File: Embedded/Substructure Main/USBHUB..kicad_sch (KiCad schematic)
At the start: 19 parts, among them U4 USB2513B_Bi, Y1 24MHz 18pF

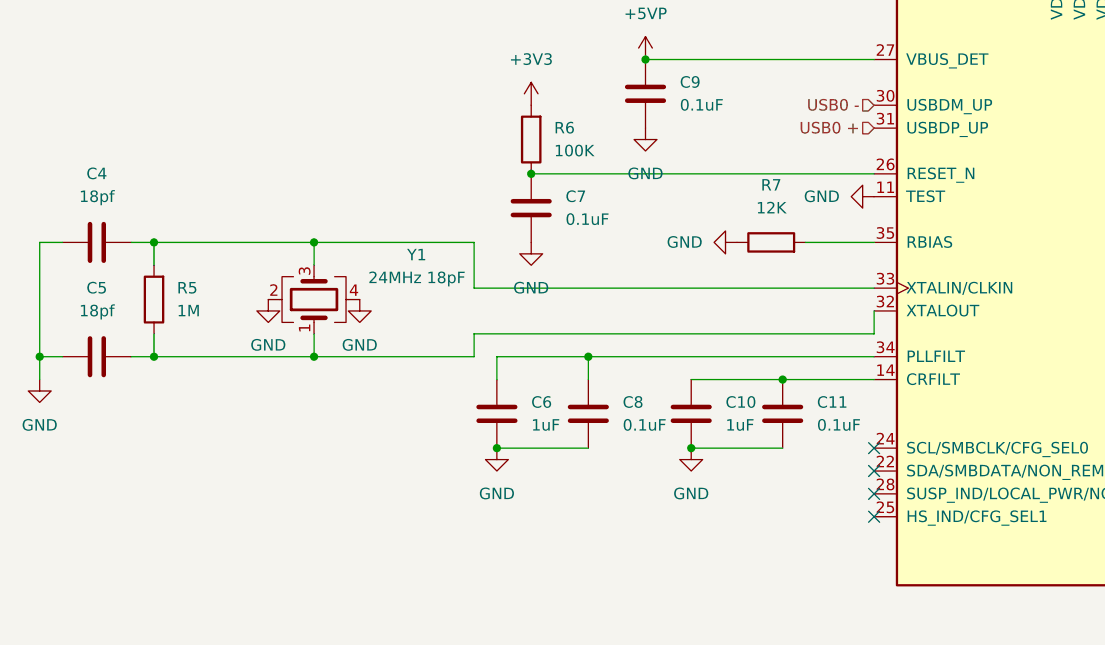
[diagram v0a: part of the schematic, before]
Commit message: Added LDOs and Modified Component Names
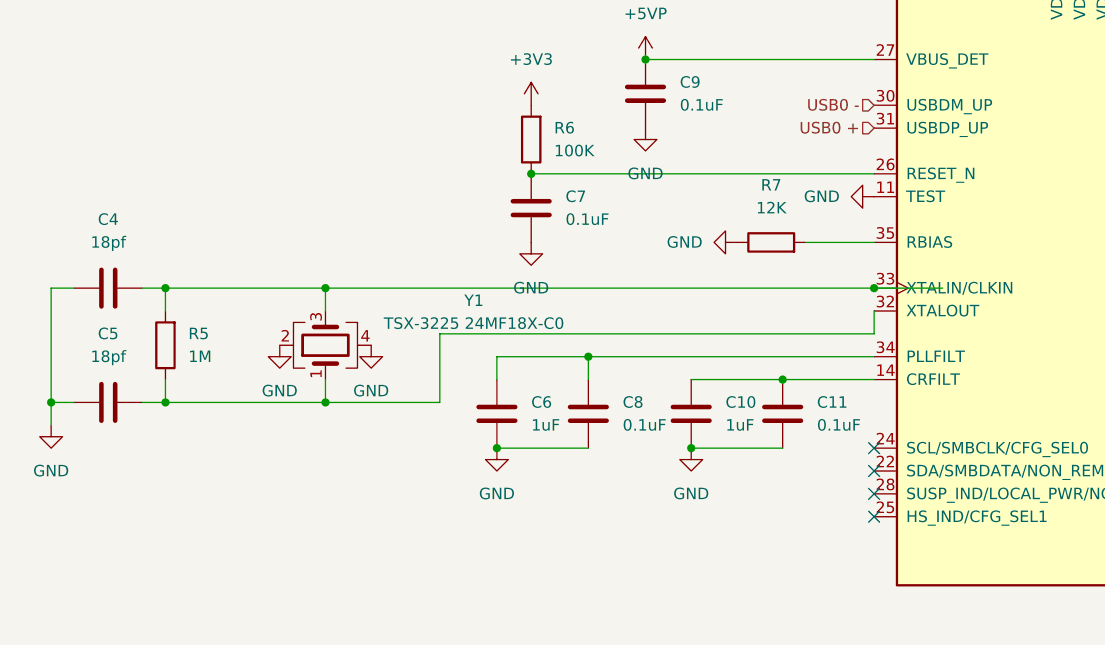
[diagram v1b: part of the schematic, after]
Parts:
- Y1: value 24MHz 18pF -> TSX-3225 24MF18X-C0
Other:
- moved on the sheet: C4, C5, R5, Y1

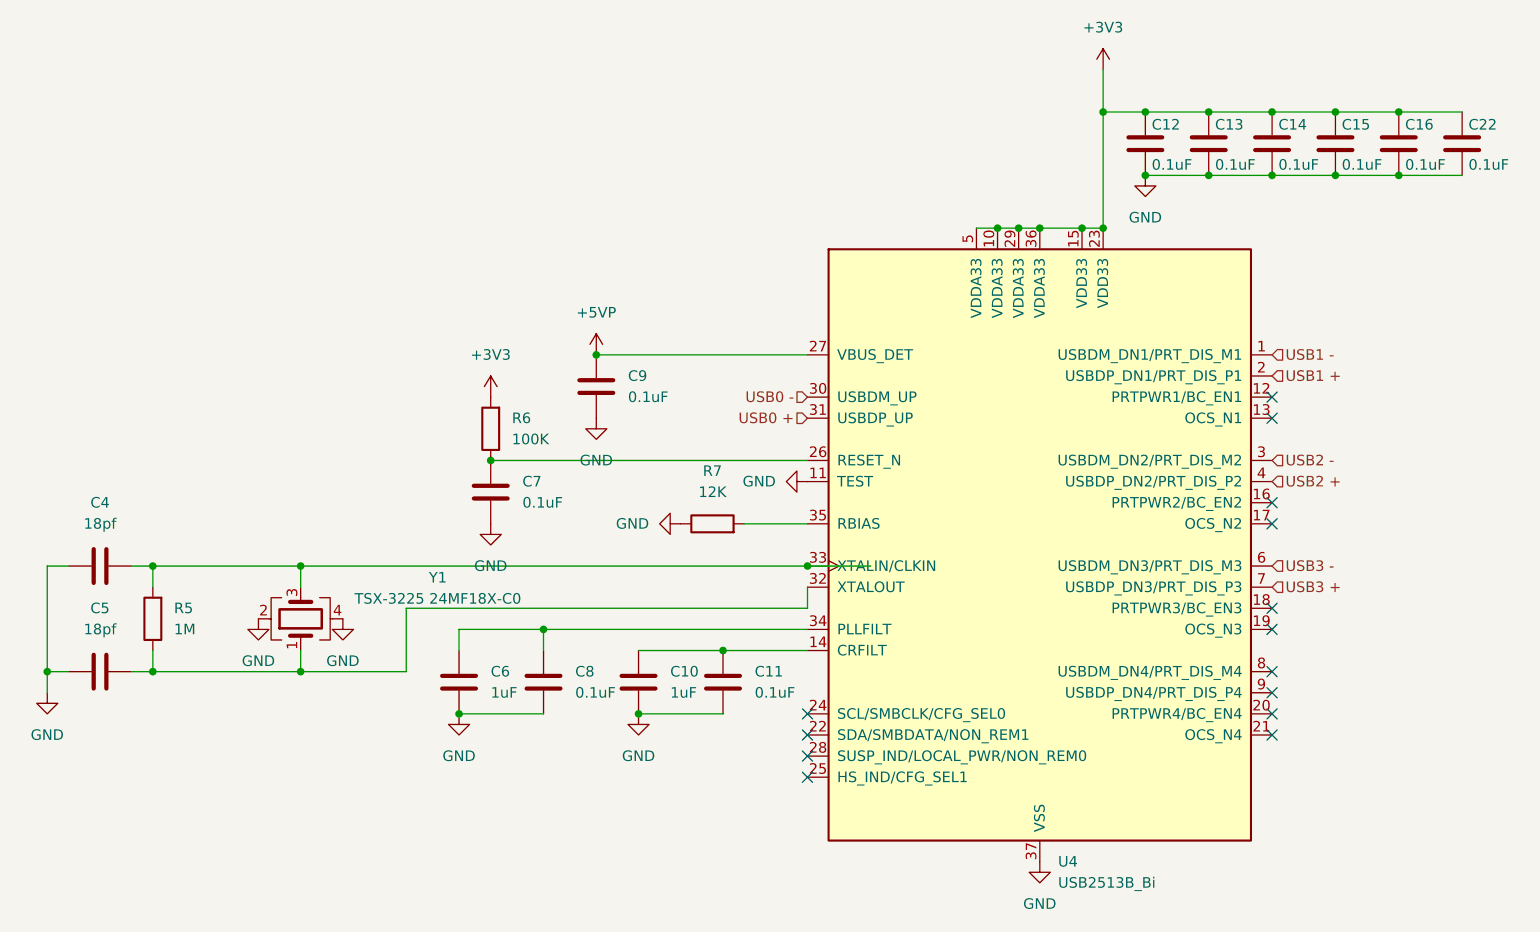
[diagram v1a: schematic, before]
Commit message: Added Sensored V2 Board
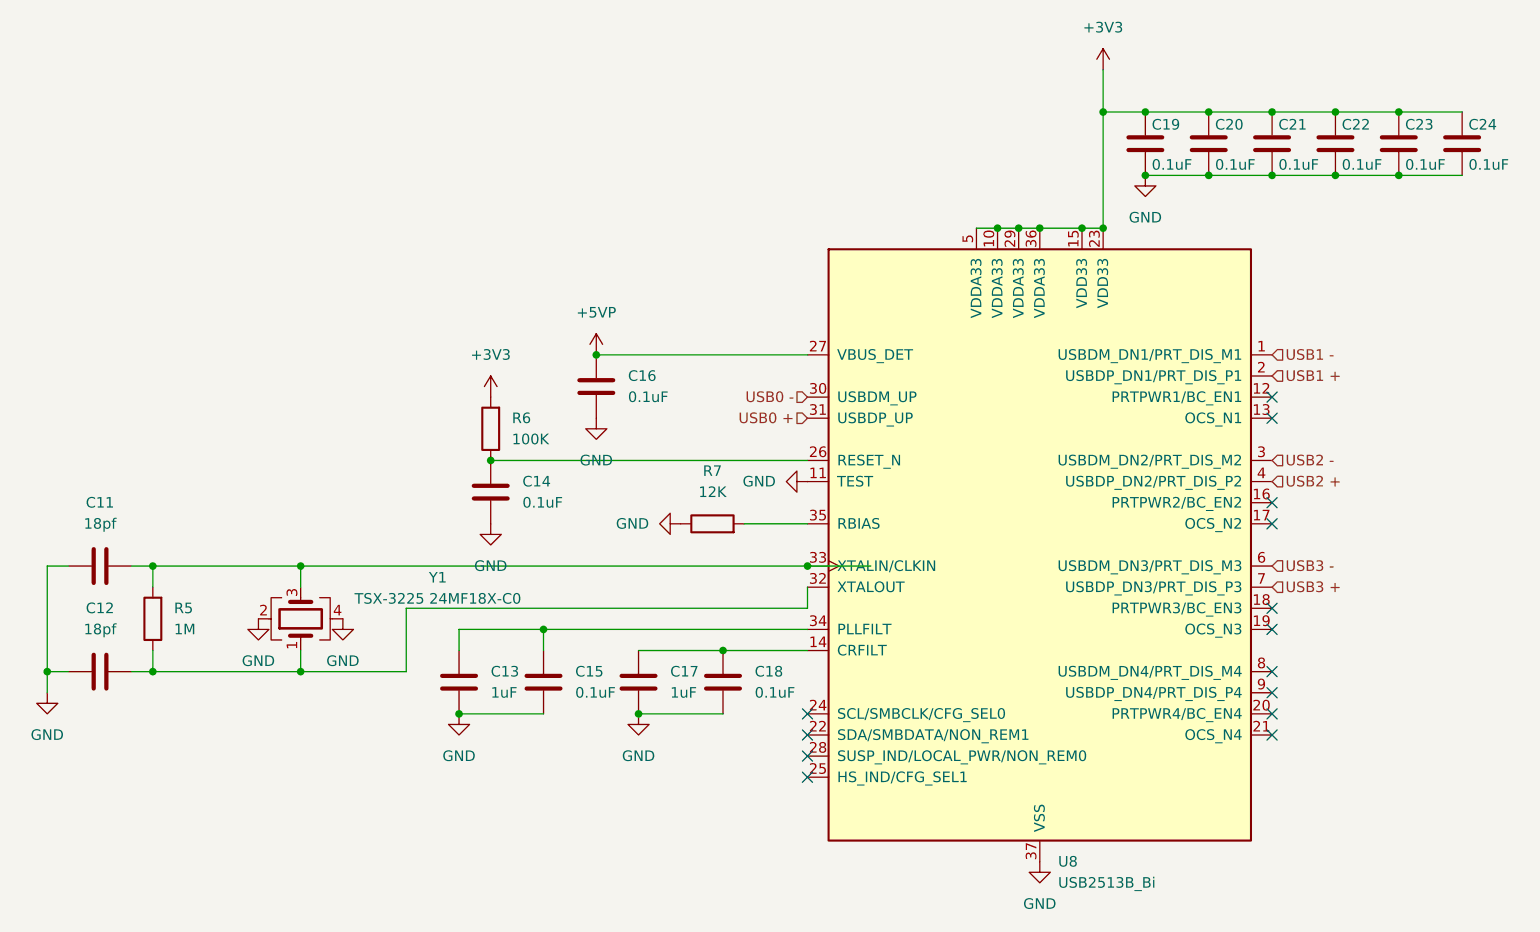
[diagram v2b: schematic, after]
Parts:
- renumbered C4 to C11, C5 to C12, C6 to C13, C7 to C14, C8 to C15, C9 to C16, C10 to C17, C11 to C18, C12 to C19, C13 to C20, C14 to C21, C15 to C22, C16 to C23, C22 to C24, U4 to U8
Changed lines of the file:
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@@
 		(dnp no)
 		(fields_autoplaced yes)
-		(property "Reference" "C4"
+		(property "Reference" "C11"
 			(at 77.47 93.98 90)
 			(effects
@@
 			(project "Substructure Main"
 				(path "/dda3f9ed-866a-496e-a4f2-d6745d13652e/a7829927-327b-42f0-a55d-415bcb49fdc6"
-					(reference "C4")
+					(reference "C11")
 					(unit 1)
 				)
@@
 		(dnp no)
 		(fields_autoplaced yes)
-		(property "Reference" "C8"
+		(property "Reference" "C15"
 			(at 134.62 114.2999 0)
 			(effects
@@
 			(project "Substructure Main"
 				(path "/dda3f9ed-866a-496e-a4f2-d6745d13652e/a7829927-327b-42f0-a55d-415bcb49fdc6"
-					(reference "C8")
+					(reference "C15")
 					(unit 1)
 				)
@@
 		(on_board yes)
 		(dnp no)
-		(property "Reference" "C15"
+		(property "Reference" "C22"
 			(at 226.822 48.514 0)
 			(effects
@@
 			(project "Substructure Main"
 				(path "/dda3f9ed-866a-496e-a4f2-d6745d13652e/a7829927-327b-42f0-a55d-415bcb49fdc6"
-					(reference "C15")
+					(reference "C22")
 					(unit 1)
 				)
@@
 		(on_board yes)
 		(dnp no)
-		(property "Reference" "C14"
+		(property "Reference" "C21"
 			(at 219.202 48.514 0)
 			(effects
@@
 			(project "Substructure Main"
 				(path "/dda3f9ed-866a-496e-a4f2-d6745d13652e/a7829927-327b-42f0-a55d-415bcb49fdc6"
-					(reference "C14")
+					(reference "C21")
 					(unit 1)
 				)
@@
 		(dnp no)
 		(fields_autoplaced yes)
-		(property "Reference" "#PWR041"
+		(property "Reference" "#PWR061"
 			(at 137.16 90.17 0)
 			(effects
@@
 			(project "Substructure Main"
 				(path "/dda3f9ed-866a-496e-a4f2-d6745d13652e/a7829927-327b-42f0-a55d-415bcb49fdc6"
-					(reference "#PWR041")
+					(reference "#PWR061")
 					(unit 1)
 				)
@@
 		(dnp no)
 		(fields_autoplaced yes)
-		(property "Reference" "C9"
+		(property "Reference" "C16"
 			(at 140.97 78.7399 0)
 			(effects
@@
 			(project "Substructure Main"
 				(path "/dda3f9ed-866a-496e-a4f2-d6745d13652e/a7829927-327b-42f0-a55d-415bcb49fdc6"
-					(reference "C9")
+					(reference "C16")
 					(unit 1)
 				)
@@
 		(dnp no)
 		(fields_autoplaced yes)
-		(property "Reference" "#PWR037"
+		(property "Reference" "#PWR057"
 			(at 120.65 125.73 0)
 			(effects
@@
 			(project "Substructure Main"
 				(path "/dda3f9ed-866a-496e-a4f2-d6745d13652e/a7829927-327b-42f0-a55d-415bcb49fdc6"
-					(reference "#PWR037")
+					(reference "#PWR057")
 					(unit 1)
 				)
@@
 		(on_board yes)
 		(dnp no)
-		(property "Reference" "C22"
+		(property "Reference" "C24"
 			(at 242.062 48.514 0)
 			(effects
@@
 			(project "Substructure Main"
 				(path "/dda3f9ed-866a-496e-a4f2-d6745d13652e/a7829927-327b-42f0-a55d-415bcb49fdc6"
-					(reference "C22")
+					(reference "C24")
 					(unit 1)
 				)
@@
 		(dnp no)
 		(fields_autoplaced yes)
-		(property "Reference" "#PWR031"
+		(property "Reference" "#PWR054"
 			(at 71.12 123.19 0)
 			(effects
@@
 			(project "Substructure Main"
 				(path "/dda3f9ed-866a-496e-a4f2-d6745d13652e/a7829927-327b-42f0-a55d-415bcb49fdc6"
-					(reference "#PWR031")
+					(reference "#PWR054")
 					(unit 1)
 				)
@@
 		(dnp no)
 		(fields_autoplaced yes)
-		(property "Reference" "#PWR036"
+		(property "Reference" "#PWR056"
 			(at 106.68 114.3 0)
 			(effects
@@
 			(project "Substructure Main"
 				(path "/dda3f9ed-866a-496e-a4f2-d6745d13652e/a7829927-327b-42f0-a55d-415bcb49fdc6"
-					(reference "#PWR036")
+					(reference "#PWR056")
 					(unit 1)
 				)
@@
 		(dnp no)
 		(fields_autoplaced yes)
-		(property "Reference" "#PWR039"
+		(property "Reference" "#PWR059"
 			(at 124.46 102.87 0)
 			(effects
@@
 			(project "Substructure Main"
 				(path "/dda3f9ed-866a-496e-a4f2-d6745d13652e/a7829927-327b-42f0-a55d-415bcb49fdc6"
-					(reference "#PWR039")
+					(reference "#PWR059")
 					(unit 1)
 				)
@@
 		(dnp no)
 		(fields_autoplaced yes)
-		(property "Reference" "#PWR044"
+		(property "Reference" "#PWR064"
 			(at 156.21 91.44 0)
 			(effects
@@
 			(project "Substructure Main"
 				(path "/dda3f9ed-866a-496e-a4f2-d6745d13652e/a7829927-327b-42f0-a55d-415bcb49fdc6"
-					(reference "#PWR044")
+					(reference "#PWR064")
 					(unit 1)
 				)
@@
 		(dnp no)
 		(fields_autoplaced yes)
-		(property "Reference" "#PWR070"
+		(property "Reference" "#PWR067"
 			(at 203.2 60.96 0)
 			(effects
@@
 			(project "Substructure Main"
 				(path "/dda3f9ed-866a-496e-a4f2-d6745d13652e/a7829927-327b-42f0-a55d-415bcb49fdc6"
-					(reference "#PWR070")
+					(reference "#PWR067")
 					(unit 1)
 				)
@@
 		(on_board yes)
 		(dnp no)
-		(property "Reference" "C12"
+		(property "Reference" "C19"
 			(at 203.962 48.514 0)
 			(effects
@@
 			(project "Substructure Main"
 				(path "/dda3f9ed-866a-496e-a4f2-d6745d13652e/a7829927-327b-42f0-a55d-415bcb49fdc6"
-					(reference "C12")
+					(reference "C19")
 					(unit 1)
 				)
@@
 		(dnp no)
 		(fields_autoplaced yes)
-		(property "Reference" "#PWR032"
+		(property "Reference" "#PWR055"
 			(at 96.52 114.3 0)
 			(effects
@@
 			(project "Substructure Main"
 				(path "/dda3f9ed-866a-496e-a4f2-d6745d13652e/a7829927-327b-42f0-a55d-415bcb49fdc6"
-					(reference "#PWR032")
+					(reference "#PWR055")
 					(unit 1)
 				)
@@
 		(dnp no)
 		(fields_autoplaced yes)
-		(property "Reference" "#PWR043"
+		(property "Reference" "#PWR063"
 			(at 140.97 96.52 0)
 			(effects
@@
 			(project "Substructure Main"
 				(path "/dda3f9ed-866a-496e-a4f2-d6745d13652e/a7829927-327b-42f0-a55d-415bcb49fdc6"
-					(reference "#PWR043")
+					(reference "#PWR063")
 					(unit 1)
 				)
@@
 		(on_board yes)
 		(dnp no)
-		(property "Reference" "C16"
+		(property "Reference" "C23"
 			(at 234.442 48.514 0)
 			(effects
@@
 			(project "Substructure Main"
 				(path "/dda3f9ed-866a-496e-a4f2-d6745d13652e/a7829927-327b-42f0-a55d-415bcb49fdc6"
-					(reference "C16")
+					(reference "C23")
 					(unit 1)
 				)
@@
 		(dnp no)
 		(fields_autoplaced yes)
-		(property "Reference" "C5"
+		(property "Reference" "C12"
 			(at 77.47 106.68 90)
 			(effects
@@
 			(project "Substructure Main"
 				(path "/dda3f9ed-866a-496e-a4f2-d6745d13652e/a7829927-327b-42f0-a55d-415bcb49fdc6"
-					(reference "C5")
+					(reference "C12")
 					(unit 1)
 				)
@@
 		(dnp no)
 		(fields_autoplaced yes)
-		(property "Reference" "C10"
+		(property "Reference" "C17"
 			(at 146.05 114.2999 0)
 			(effects
@@
 			(project "Substructure Main"
 				(path "/dda3f9ed-866a-496e-a4f2-d6745d13652e/a7829927-327b-42f0-a55d-415bcb49fdc6"
-					(reference "C10")
+					(reference "C17")
 					(unit 1)
 				)
@@
 		(dnp no)
 		(fields_autoplaced yes)
-		(property "Reference" "U4"
+		(property "Reference" "U8"
 			(at 192.6941 137.16 0)
 			(effects
@@
 			(project "Substructure Main"
 				(path "/dda3f9ed-866a-496e-a4f2-d6745d13652e/a7829927-327b-42f0-a55d-415bcb49fdc6"
-					(reference "U4")
+					(reference "U8")
 					(unit 1)
 				)
@@
 		(dnp no)
 		(fields_autoplaced yes)
-		(property "Reference" "#PWR069"
+		(property "Reference" "#PWR066"
 			(at 198.12 45.72 0)
 			(effects
@@
 			(project "Substructure Main"
 				(path "/dda3f9ed-866a-496e-a4f2-d6745d13652e/a7829927-327b-42f0-a55d-415bcb49fdc6"
-					(reference "#PWR069")
+					(reference "#PWR066")
 					(unit 1)
 				)
@@
 		(on_board yes)
 		(dnp no)
-		(property "Reference" "C13"
+		(property "Reference" "C20"
 			(at 211.582 48.514 0)
 			(effects
@@
 			(project "Substructure Main"
 				(path "/dda3f9ed-866a-496e-a4f2-d6745d13652e/a7829927-327b-42f0-a55d-415bcb49fdc6"
-					(reference "C13")
+					(reference "C20")
 					(unit 1)
 				)
@@
 		(dnp no)
 		(fields_autoplaced yes)
-		(property "Reference" "#PWR038"
+		(property "Reference" "#PWR058"
 			(at 124.46 85.09 0)
 			(effects
@@
 			(project "Substructure Main"
 				(path "/dda3f9ed-866a-496e-a4f2-d6745d13652e/a7829927-327b-42f0-a55d-415bcb49fdc6"
-					(reference "#PWR038")
+					(reference "#PWR058")
 					(unit 1)
 				)
@@
 		(dnp no)
 		(fields_autoplaced yes)
-		(property "Reference" "#PWR040"
+		(property "Reference" "#PWR060"
 			(at 137.16 80.01 0)
 			(effects
@@
 			(project "Substructure Main"
 				(path "/dda3f9ed-866a-496e-a4f2-d6745d13652e/a7829927-327b-42f0-a55d-415bcb49fdc6"
-					(reference "#PWR040")
+					(reference "#PWR060")
 					(unit 1)
 				)
@@
 		(dnp no)
 		(fields_autoplaced yes)
-		(property "Reference" "C6"
+		(property "Reference" "C13"
 			(at 124.46 114.2999 0)
 			(effects
@@
 			(project "Substructure Main"
 				(path "/dda3f9ed-866a-496e-a4f2-d6745d13652e/a7829927-327b-42f0-a55d-415bcb49fdc6"
-					(reference "C6")
+					(reference "C13")
 					(unit 1)
 				)
@@
 		(dnp no)
 		(fields_autoplaced yes)
-		(property "Reference" "#PWR055"
+		(property "Reference" "#PWR065"
 			(at 190.5 143.51 0)
 			(effects
@@
 			(project "Substructure Main"
 				(path "/dda3f9ed-866a-496e-a4f2-d6745d13652e/a7829927-327b-42f0-a55d-415bcb49fdc6"
-					(reference "#PWR055")
+					(reference "#PWR065")
 					(unit 1)
 				)
@@
 		(dnp no)
 		(fields_autoplaced yes)
-		(property "Reference" "#PWR042"
+		(property "Reference" "#PWR062"
 			(at 142.24 125.73 0)
 			(effects
@@
 			(project "Substructure Main"
 				(path "/dda3f9ed-866a-496e-a4f2-d6745d13652e/a7829927-327b-42f0-a55d-415bcb49fdc6"
-					(reference "#PWR042")
+					(reference "#PWR062")
 					(unit 1)
 				)
@@
 		(dnp no)
 		(fields_autoplaced yes)
-		(property "Reference" "C7"
+		(property "Reference" "C14"
 			(at 128.27 91.4399 0)
 			(effects
@@
 			(project "Substructure Main"
 				(path "/dda3f9ed-866a-496e-a4f2-d6745d13652e/a7829927-327b-42f0-a55d-415bcb49fdc6"
-					(reference "C7")
+					(reference "C14")
 					(unit 1)
 				)
@@
 		(dnp no)
 		(fields_autoplaced yes)
-		(property "Reference" "C11"
+		(property "Reference" "C18"
 			(at 156.21 114.2999 0)
 			(effects
@@
 			(project "Substructure Main"
 				(path "/dda3f9ed-866a-496e-a4f2-d6745d13652e/a7829927-327b-42f0-a55d-415bcb49fdc6"
-					(reference "C11")
-					(unit 1)
-				)
+					(reference "C18")
+					(unit 1)
+				)

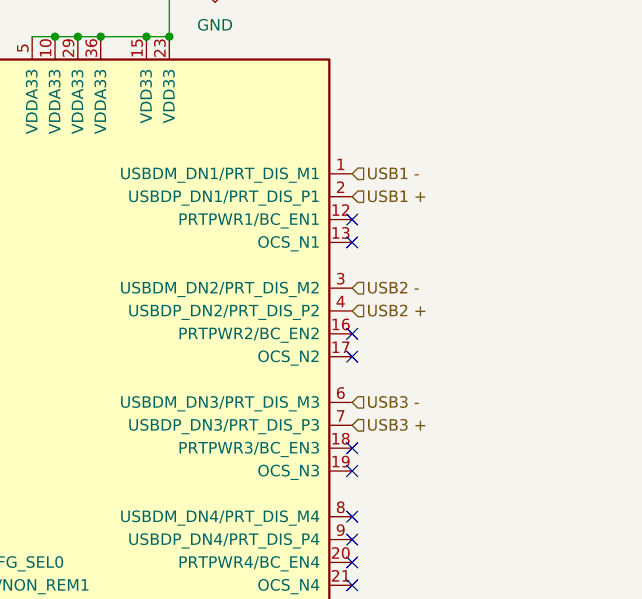
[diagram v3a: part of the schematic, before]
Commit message: Modified Board from 2 Layer to 4 Layers & Routed close components
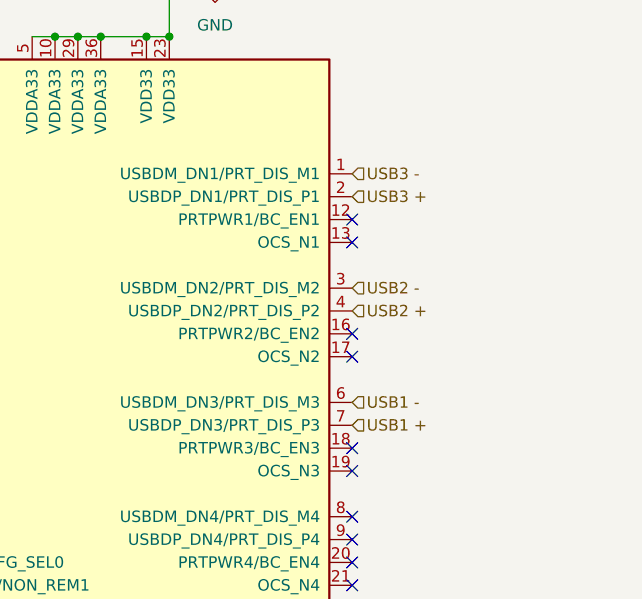
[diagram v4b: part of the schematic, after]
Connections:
- net USB1 +: now also U8.7 (USBDP_DN3/PRT_DIS_P3); no longer U8.2 (USBDP_DN1/PRT_DIS_P1)
- net USB1 -: now also U8.6 (USBDM_DN3/PRT_DIS_M3); no longer U8.1 (USBDM_DN1/PRT_DIS_M1)
- net USB3 +: now also U8.2 (USBDP_DN1/PRT_DIS_P1); no longer U8.7 (USBDP_DN3/PRT_DIS_P3)
- net USB3 -: now also U8.1 (USBDM_DN1/PRT_DIS_M1); no longer U8.6 (USBDM_DN3/PRT_DIS_M3)
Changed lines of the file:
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@@
 	(hierarchical_label "USB3 -"
 		(shape input)
-		(at 218.44 101.6 0)
+		(at 218.44 76.2 0)
 		(effects
 			(font
@@
 	(hierarchical_label "USB1 +"
 		(shape input)
-		(at 218.44 78.74 0)
+		(at 218.44 104.14 0)
 		(effects
 			(font
@@
 	(hierarchical_label "USB1 -"
 		(shape input)
-		(at 218.44 76.2 0)
+		(at 218.44 101.6 0)
 		(effects
 			(font
@@
 	(hierarchical_label "USB3 +"
 		(shape input)
-		(at 218.44 104.14 0)
+		(at 218.44 78.74 0)
 		(effects
 			(font
